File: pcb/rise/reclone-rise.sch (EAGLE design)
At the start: 130 parts, among them Y1 12MHz

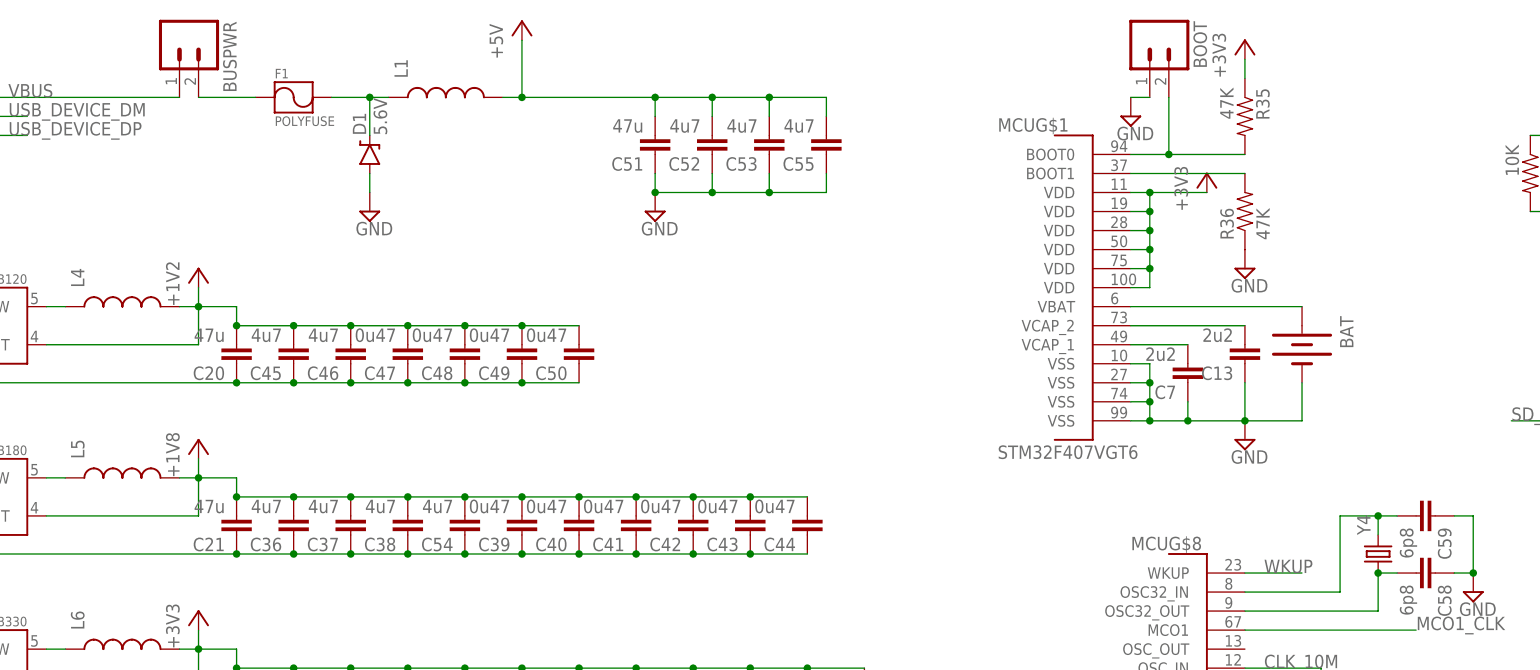
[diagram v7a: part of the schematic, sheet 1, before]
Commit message: Fixed a few ERC issues
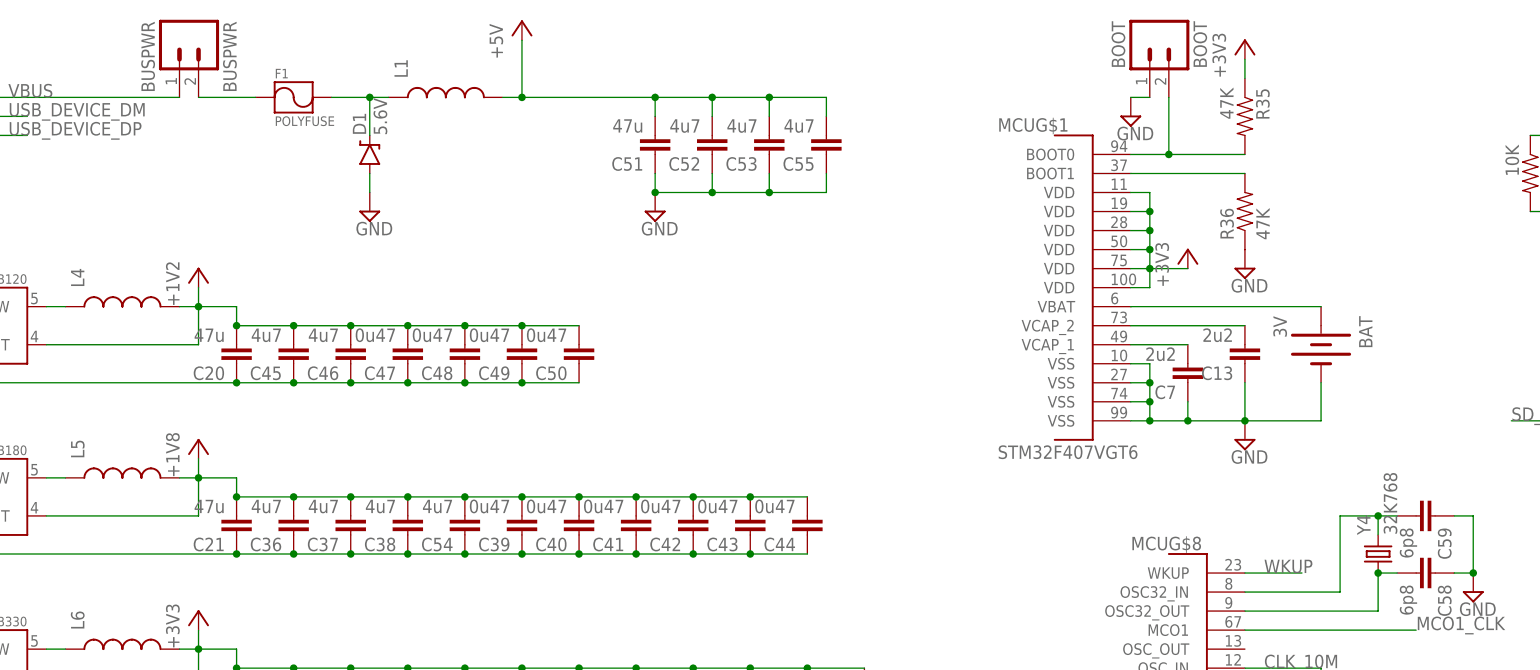
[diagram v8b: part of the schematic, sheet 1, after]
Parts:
- BAT: value (none) -> 3V
- BOOT: value (none) -> BOOT
- BUSPWR: value (none) -> BUSPWR
- Y4: value (none) -> 32K768
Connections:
- net GPIO25: now also FPGAB0.IO_L66N_SCP0_0
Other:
- moved on the sheet: BAT
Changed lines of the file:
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@@
 <part name="P+6" library="supply1" deviceset="+5V" device=""/>
 <part name="R19" library="SparkFun-Passives" deviceset="RESISTOR" device="0603-RES" value="4"/>
-<part name="FRAME1" library="frames" deviceset="A3L-LOC" device=""/>
-<part name="FRAME2" library="frames" deviceset="A3L-LOC" device=""/>
+<part name="FRAME1" library="frames" deviceset="A3L-LOC" device="" value="SHEET1"/>
+<part name="FRAME2" library="frames" deviceset="A3L-LOC" device="" value="SHEET2"/>
 <part name="+3V19" library="supply1" deviceset="+3V3" device=""/>
 <part name="+3V20" library="supply1" deviceset="+3V3" device=""/>
@@
 <part name="C7" library="SparkFun-Passives" deviceset="CAP" device="0603-CAP" value="2u2"/>
 <part name="C13" library="SparkFun-Passives" deviceset="CAP" device="0603-CAP" value="2u2"/>
-<part name="BOOT" library="SparkFun-Connectors" deviceset="M02" device="PTH"/>
-<part name="BUSPWR" library="SparkFun-Connectors" deviceset="M02" device="PTH"/>
+<part name="BOOT" library="SparkFun-Connectors" deviceset="M02" device="PTH" value="BOOT"/>
+<part name="BUSPWR" library="SparkFun-Connectors" deviceset="M02" device="PTH" value="BUSPWR"/>
 <part name="SUPPLY26" library="supply2" deviceset="GND" device=""/>
 <part name="SUPPLY27" library="supply2" deviceset="GND" device=""/>
@@
 <part name="C54" library="SparkFun-Passives" deviceset="CAP" device="0603-CAP" value="4u7"/>
 <part name="C55" library="SparkFun-Passives" deviceset="CAP" device="0603-CAP" value="4u7"/>
-<part name="BAT" library="SparkFun-Electromechanical" deviceset="BATTERY" device="12MM"/>
-<part name="Y4" library="SparkFun-FreqCtrl" deviceset="CRYSTAL" device="EPSONMC146"/>
+<part name="BAT" library="SparkFun-Electromechanical" deviceset="BATTERY" device="12MM" value="3V"/>
+<part name="Y4" library="SparkFun-FreqCtrl" deviceset="CRYSTAL" device="EPSONMC146" value="32K768"/>
 <part name="C58" library="SparkFun-Passives" deviceset="CAP" device="0603-CAP" value="6p8"/>
 <part name="C59" library="SparkFun-Passives" deviceset="CAP" device="0603-CAP" value="6p8"/>
@@
 <instance part="SUPPLY14" gate="GND" x="365.76" y="167.64"/>
 <instance part="SUPPLY15" gate="GND" x="213.36" y="190.5"/>
-<instance part="+3V9" gate="G$1" x="208.28" y="226.06"/>
+<instance part="+3V9" gate="G$1" x="205.74" y="215.9"/>
 <instance part="R14" gate="G$1" x="111.76" y="35.56" rot="R90"/>
 <instance part="TXRX" gate="G$1" x="111.76" y="45.72"/>
@@
 <instance part="C54" gate="G$1" x="109.22" y="180.34" rot="R180"/>
 <instance part="C55" gate="G$1" x="157.48" y="231.14" rot="R180"/>
-<instance part="BAT" gate="G$1" x="220.98" y="203.2" rot="R270"/>
+<instance part="BAT" gate="G$1" x="223.52" y="203.2" rot="R270"/>
 <instance part="Y4" gate="G$1" x="231.14" y="175.26" rot="R90"/>
 <instance part="C58" gate="G$1" x="236.22" y="172.72" rot="R270"/>
@@
 <junction x="213.36" y="193.04"/>
 <pinref part="BAT" gate="G$1" pin="-"/>
-<wire x1="220.98" y1="198.12" x2="220.98" y2="193.04" width="0.1524" layer="91"/>
-<wire x1="220.98" y1="193.04" x2="213.36" y2="193.04" width="0.1524" layer="91"/>
+<wire x1="223.52" y1="198.12" x2="223.52" y2="193.04" width="0.1524" layer="91"/>
+<wire x1="223.52" y1="193.04" x2="213.36" y2="193.04" width="0.1524" layer="91"/>
 </segment>
 <segment>
@@
 </segment>
 <segment>
-<pinref part="MCU" gate="G$1" pin="VDD@100"/>
-<wire x1="198.12" y1="210.82" x2="200.66" y2="210.82" width="0.1524" layer="91"/>
-<wire x1="200.66" y1="210.82" x2="200.66" y2="213.36" width="0.1524" layer="91"/>
-<pinref part="+3V9" gate="G$1" pin="+3V3"/>
-<wire x1="200.66" y1="213.36" x2="200.66" y2="215.9" width="0.1524" layer="91"/>
-<wire x1="200.66" y1="215.9" x2="200.66" y2="218.44" width="0.1524" layer="91"/>
-<wire x1="200.66" y1="218.44" x2="200.66" y2="220.98" width="0.1524" layer="91"/>
-<wire x1="200.66" y1="220.98" x2="200.66" y2="223.52" width="0.1524" layer="91"/>
-<wire x1="200.66" y1="223.52" x2="208.28" y2="223.52" width="0.1524" layer="91"/>
-<pinref part="MCU" gate="G$1" pin="VDD@11"/>
-<wire x1="198.12" y1="223.52" x2="200.66" y2="223.52" width="0.1524" layer="91"/>
-<pinref part="MCU" gate="G$1" pin="VDD@19"/>
-<wire x1="198.12" y1="220.98" x2="200.66" y2="220.98" width="0.1524" layer="91"/>
-<pinref part="MCU" gate="G$1" pin="VDD@28"/>
-<wire x1="198.12" y1="218.44" x2="200.66" y2="218.44" width="0.1524" layer="91"/>
-<pinref part="MCU" gate="G$1" pin="VDD@50"/>
-<wire x1="198.12" y1="215.9" x2="200.66" y2="215.9" width="0.1524" layer="91"/>
-<pinref part="MCU" gate="G$1" pin="VDD@75"/>
-<wire x1="198.12" y1="213.36" x2="200.66" y2="213.36" width="0.1524" layer="91"/>
-<junction x="200.66" y="223.52"/>
-<junction x="200.66" y="220.98"/>
-<junction x="200.66" y="218.44"/>
-<junction x="200.66" y="215.9"/>
-<junction x="200.66" y="213.36"/>
-</segment>
-<segment>
 <pinref part="TXRX" gate="G$1" pin="A"/>
 <pinref part="+3V10" gate="G$1" pin="+3V3"/>
@@
 <wire x1="198.12" y1="144.78" x2="200.66" y2="144.78" width="0.1524" layer="91"/>
 </segment>
+<segment>
+<pinref part="MCU" gate="G$1" pin="VDD@100"/>
+<wire x1="198.12" y1="210.82" x2="200.66" y2="210.82" width="0.1524" layer="91"/>
+<wire x1="200.66" y1="210.82" x2="200.66" y2="213.36" width="0.1524" layer="91"/>
+<wire x1="200.66" y1="213.36" x2="200.66" y2="215.9" width="0.1524" layer="91"/>
+<wire x1="200.66" y1="215.9" x2="200.66" y2="218.44" width="0.1524" layer="91"/>
+<wire x1="200.66" y1="218.44" x2="200.66" y2="220.98" width="0.1524" layer="91"/>
+<wire x1="200.66" y1="220.98" x2="200.66" y2="223.52" width="0.1524" layer="91"/>
+<pinref part="MCU" gate="G$1" pin="VDD@11"/>
+<wire x1="198.12" y1="223.52" x2="200.66" y2="223.52" width="0.1524" layer="91"/>
+<pinref part="MCU" gate="G$1" pin="VDD@19"/>
+<wire x1="198.12" y1="220.98" x2="200.66" y2="220.98" width="0.1524" layer="91"/>
+<pinref part="MCU" gate="G$1" pin="VDD@28"/>
+<wire x1="198.12" y1="218.44" x2="200.66" y2="218.44" width="0.1524" layer="91"/>
+<pinref part="MCU" gate="G$1" pin="VDD@50"/>
+<wire x1="198.12" y1="215.9" x2="200.66" y2="215.9" width="0.1524" layer="91"/>
+<pinref part="MCU" gate="G$1" pin="VDD@75"/>
+<wire x1="198.12" y1="213.36" x2="200.66" y2="213.36" width="0.1524" layer="91"/>
+<junction x="200.66" y="220.98"/>
+<junction x="200.66" y="218.44"/>
+<junction x="200.66" y="215.9"/>
+<junction x="200.66" y="213.36"/>
+<pinref part="+3V9" gate="G$1" pin="+3V3"/>
+<wire x1="200.66" y1="213.36" x2="205.74" y2="213.36" width="0.1524" layer="91"/>
+</segment>
 </net>
 <net name="FPGA_CONFIG_CLK" class="0">
@@
 <pinref part="MCU" gate="G$1" pin="VBAT"/>
 <pinref part="BAT" gate="G$1" pin="+"/>
-<wire x1="198.12" y1="208.28" x2="220.98" y2="208.28" width="0.1524" layer="91"/>
+<wire x1="198.12" y1="208.28" x2="223.52" y2="208.28" width="0.1524" layer="91"/>
 </segment>
 </net>
@@
 <label x="22.86" y="187.96" size="1.778" layer="95"/>
 </segment>
+<segment>
+<pinref part="FPGA" gate="B0" pin="IO_L66N_SCP0_0"/>
+<wire x1="38.1" y1="17.78" x2="40.64" y2="17.78" width="0.1524" layer="91"/>
+<label x="40.64" y="17.78" size="1.778" layer="95"/>
+</segment>
 </net>
 <net name="GPIO26" class="0">
@@
 </sheet>
 </sheets>
+<errors>
+</errors>
 </schematic>
 </drawing>
